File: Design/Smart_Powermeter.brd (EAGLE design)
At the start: 92 x 87 mm, 66 parts, among them IC1 AMS1117-3.3, IC3 ESP32-S2-MINI-1-N4R2, J1 AUDIO_JACK_TRRSSMD_RA, J2 AUDIO_JACK_TRRSSMD_RA, J3 AUDIO_JACK_TRRSSMD_RA, J4 AUDIO_JACK_TRRSSMD_RA, J5 AUDIO_JACK_TRRSSMD_RA, J6 AUDIO_JACK_TRRSSMD_RA, J8 USB-C, Q1 IRLML0100

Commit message: First draft for the Pro version
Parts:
- removed X1: (no value), con-wago-508:W237-132
- added C16, C20, C21: 10u/6V, rcl:C0603
- added D4, D5, D7: ESD5Z3.3T1G, microbuilder:SOD-523
- added F1, F2, F3: 1A x 250V, OpenEnergyMonitor:FUSE
- added JP1, JP2, JP3, JP4, JP5, JP6: JUMPER-SMT_2_NC_TRACE_NO-SILK, SparkFun-Jumpers:SMT-JUMPER_2_NC_TRACE_NO-SILK
- added M1, M2, M3: 275VAC, OpenEnergyMonitor:MOV
- added R21, R22, R23, R24, R26, R27, R28, R32, R33, R34, R35, R38, R39, R40, R48, R49, R50, R51, R52, R53, R54: 10k, rcl:R0603
- added R29, R41, R55: 180k, rcl:R0603
- added R30, R42, R56: 33k, rcl:R0603
- added R31, R43, R57: 1k, rcl:R0603
- added T1, T2, T3: ZMPT101B, OpenEnergyMonitor:ZMPT101B
- added X2: (no value), con-wago-508:W237-5P
- J1, J2, J3, J4, J5, J6: value AUDIO_JACK_TRRSSMD_RA -> AUDIO_JACK_MONO_3.5_3P; device SparkFun-Connectors:AUDIO_JACK_3.5MM_TRRS_SMD_RA -> SpaceDIY_connectors:HC-PJ-320A-3P-D
- R10, R13, R16, R19, R4, R7: device rcl:R1206 -> rcl:R0603
- moved J4 91.5 mm to (51.6, 86.0), turned to 180 degrees
- moved J5 90.5 mm to (62.8, 86.0), turned to 180 degrees
- moved J6 89.7 mm to (74.0, 86.0), turned to 180 degrees
- moved R13 84.0 mm to (46.6, 84.0), flipped to the bottom, turned to 0 degrees
- moved R16 82.9 mm to (57.8, 84.0), flipped to the bottom, turned to 0 degrees
- moved R19 81.9 mm to (69.0, 84.0), flipped to the bottom, turned to 0 degrees
- moved S1 80.3 mm to (76.0, 5.00), turned to 270 degrees
- moved S2 80.3 mm to (58.0, 5.00), turned to 270 degrees
- moved J8 71.0 mm to (67.0, 9.00), turned to 0 degrees
- moved R15 70.7 mm to (57.8, 80.0), flipped to the bottom, turned to 0 degrees
- moved U$2 70.3 mm to (19.0, 44.0), turned to 90 degrees
- moved R18 69.6 mm to (69.0, 80.0), flipped to the bottom, turned to 0 degrees
- moved R12 69.5 mm to (46.6, 80.0), flipped to the bottom, turned to 0 degrees
- moved R11 68.8 mm to (46.6, 78.0), flipped to the bottom, turned to 180 degrees
- moved C4 68.2 mm to (46.6, 76.0), flipped to the bottom, turned to 0 degrees
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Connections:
- removed net VG0: C1.1, J1.EARTH, R2.2, R3.1, R4.1
- new net L1: F1.IN, M1.1, R48.1, U$2.AC1
- new net L2: F2.IN, M2.1, R21.1
- new net L3: F3.IN, M3.1, R32.1
- new net N$10: R23.2, T2.2
- new net N$18: C20.1, R28.1, T2.3
- new net N$19: C20.2, R29.1, R30.2, R31.2
- new net N$20: R32.2, R33.1
- new net N$21: R33.2, R34.1
- new net N$22: R35.1, T3.1
- new net N$23: R35.2, R38.1
- new net N$24: R38.2, R39.1
- new net N$25: R48.2, R49.1
- new net N$26: R34.2, T3.2
- new net N$27: C21.1, R40.1, T3.3
- new net N$28: C21.2, R41.1, R42.2, R43.2
- new net N$29: JP2.2, R7.2
- new net N$3: F2.OUT, X2.2
- new net N$30: JP3.2, R10.2
- new net N$33: JP4.2, R13.2
- new net N$34: JP5.2, R16.2
- new net N$35: JP6.2, R19.2
- new net N$36: R49.2, R50.1
- new net N$37: R51.1, T1.1
- new net N$38: R51.2, R52.1
- new net N$39: R52.2, R53.1
- new net N$4: F3.OUT, X2.3
- new net N$40: R50.2, T1.2
- new net N$41: C16.1, R54.1, T1.3
- new net N$44: C16.2, R55.1, R56.2, R57.2
- new net N$5: R21.2, R22.1
- new net N$6: R22.2, R23.1
- new net N$7: R24.1, T2.1
- new net N$8: R24.2, R26.1
- new net N$9: R26.2, R27.1
- new net NEUTRAL: M1.2, M2.2, M3.2, R27.2, R39.2, R53.2, U$2.AC2, X2.4
- new net V1: D4.K, R57.1
- new net V2: D5.K, R31.1
- new net V3: D7.K, R43.1
- new net VG6: C6.1, J6.1, JP6.1, R17.2, R18.1
- net 3.3V: now also R29.2, R41.2, R55.2
- net GND: now also D4.A, D5.A, D7.A, R28.2, R30.1, R40.2, R42.1, R54.2, R56.1, T1.4, T2.4, T3.4, X2.5
- net M1: now also J1.2, J1.3, R4.1; no longer J1.RING1, J1.RING2, J1.TIP, R4.2
- net M2: now also J2.2, J2.3, R7.1; no longer J2.RING1, J2.RING2, J2.TIP, R7.2
- net M3: now also J3.2, J3.3, R10.1; no longer J3.RING1, J3.RING2, J3.TIP, R10.2
- net M4: now also J4.2, J4.3, R13.1; no longer J4.RING1, J4.RING2, J4.TIP, R13.2
- net M5: now also J5.2, J5.3, R16.1; no longer J5.RING1, J5.RING2, J5.TIP, R16.2
- net M6: now also J6.2, J6.3, R19.1; no longer J6.RING1, J6.RING2, J6.TIP, R19.2
- net N$1: now also JP1.2, R4.2; no longer U$2.AC2, X1.2
- net N$2: now also F1.OUT, X2.1; no longer U$2.AC1, X1.1
- net VG1: now also C1.1, J1.1, JP1.1, R2.2, R3.1; no longer C2.1, J2.EARTH, R5.2, R6.1, R7.1
- net VG2: now also C2.1, J2.1, JP2.1, R5.2, R6.1; no longer C3.1, J3.EARTH, R10.1, R8.2, R9.1
- net VG3: now also C3.1, J3.1, JP3.1, R8.2, R9.1; no longer C4.1, J4.EARTH, R11.2, R12.1, R13.1
- net VG4: now also C4.1, J4.1, JP4.1, R11.2, R12.1; no longer C5.1, J5.EARTH, R14.2, R15.1, R16.1
- net VG5: now also C5.1, J5.1, JP5.1, R14.2, R15.1; no longer C6.1, J6.EARTH, R17.2, R18.1, R19.1
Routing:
- net 3.3V: track 206.4 -> 325.6 mm, vias 5 -> 10
- net NEUTRAL: track 0.00 -> 109.2 mm
- net M4: track 129.1 -> 69.1 mm, vias 4 -> 3
- net L1: track 0.00 -> 57.6 mm
- net M5: track 118.0 -> 60.4 mm, vias 4 -> 3
- net M6: track 104.3 -> 48.4 mm, vias 4 -> 3
- net GND: track 7.30 -> 49.6 mm, vias 6 -> 0
- net RST: track 53.0 -> 80.6 mm, vias 2 -> 1
- net N$4: track 0.00 -> 24.3 mm
- net 5V: track 124.8 -> 148.4 mm, vias 2 -> 4
- net SPI_CS: track 72.0 -> 50.4 mm, vias 4 -> 2
- net SPI_CLK: track 65.4 -> 46.3 mm, vias 4 -> 2
- net SPI_MOSI: track 67.0 -> 49.2 mm, vias 4 -> 2
- net SPI_MISO: track 64.4 -> 46.7 mm
- net N$12: track 31.1 -> 13.7 mm, vias 0 -> 2
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
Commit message: Updated design files
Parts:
- added JP10, JP11, JP12, JP7, JP8, JP9: JUMPER-SMT_2_NO_NO-SILK, SparkFun-Jumpers:SMT-JUMPER_2_NO_NO-SILK
- added JP13: JUMPER-SMT_2_NC_PASTE_NO-SILK, SparkFun-Jumpers:SMT-JUMPER_2_NC_PASTE_NO-SILK
- added LED1: GREEN, SparkFun-LED:LED-0603
- added LED2: BLUE, SparkFun-LED:LED-0603
- added R44: 470, rcl:R0603
- added R45: 330, rcl:R0603
- moved J8 2.00 mm to (67.0, 7.00)
- moved R36 2.00 mm to (70.0, 11.0)
- moved R37 2.00 mm to (64.0, 11.0)
- moved S1 1.58 mm to (76.5, 3.50), turned to 180 degrees
- moved S2 1.58 mm to (57.5, 3.50), turned to 180 degrees
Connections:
- new net LED: IC3.12, R45.2
- new net N$42: LED1.A, R44.1
- new net N$43: JP13.2, R44.2
- new net N$45: LED2.A, R45.1
- new net N$46: J1.2, JP8.2
- new net N$47: J2.2, JP7.2
- new net N$48: J3.2, JP9.2
- new net N$49: J4.2, JP10.2
- new net N$50: J5.2, JP11.2
- new net N$51: J6.2, JP12.2
- net 3.3V: now also JP13.1
- net GND: now also LED1.C, LED2.C
- net M1: now also JP8.1; no longer J1.2
- net M2: now also JP7.1; no longer J2.2
- net M3: now also JP9.1; no longer J3.2
- net M4: now also JP10.1; no longer J4.2
- net M5: now also JP11.1; no longer J5.2
- net M6: now also JP12.1; no longer J6.2
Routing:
- net N$45: track 0.00 -> 35.3 mm, vias 0 -> 1
- net N$42: track 0.00 -> 30.9 mm, vias 0 -> 1
- net LED: track 0.00 -> 17.1 mm, vias 0 -> 2
- net N$17: track 11.0 -> 27.0 mm
- net GND: track 49.6 -> 57.0 mm, vias 0 -> 14
- net N$43: track 0.00 -> 3.04 mm
- net N$49: track 0.00 -> 2.20 mm
- net N$48: track 0.00 -> 2.20 mm
- net N$47: track 0.00 -> 2.20 mm
- net N$46: track 0.00 -> 2.20 mm
- net N$51: track 0.00 -> 2.20 mm
- net N$50: track 0.00 -> 2.20 mm
- net VG6: track 8.96 -> 11.0 mm
- net VG4: track 8.93 -> 10.9 mm
- net VG1: track 8.93 -> 10.9 mm
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
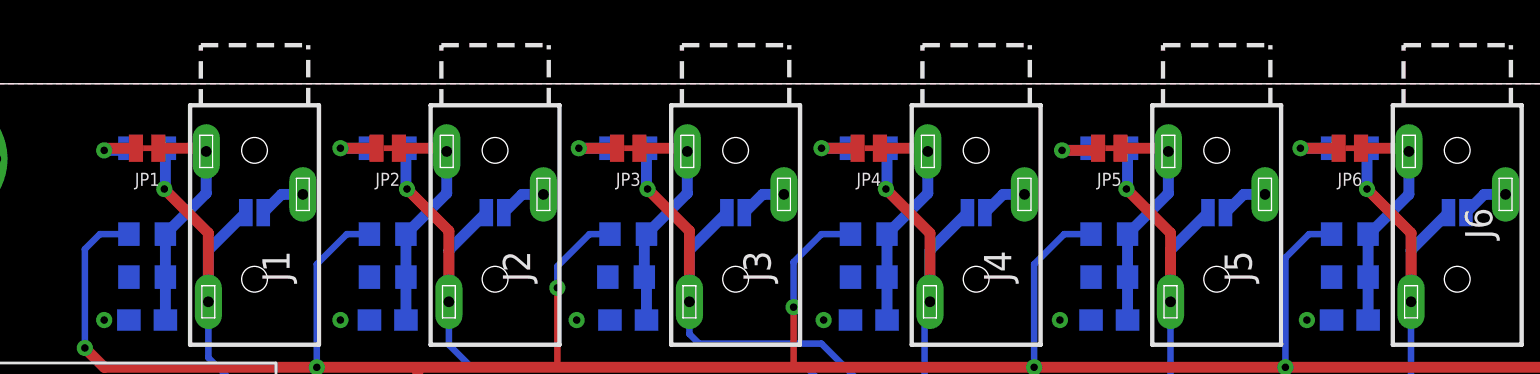
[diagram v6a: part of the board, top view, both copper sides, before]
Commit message: Smart Powermeter Pro with V/I measurements directly on the ESP32-S2
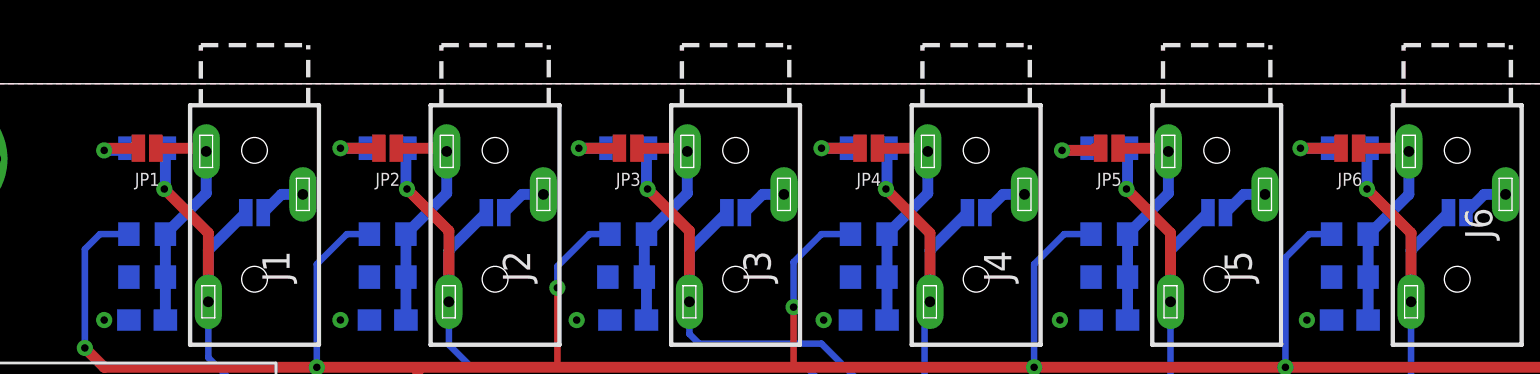
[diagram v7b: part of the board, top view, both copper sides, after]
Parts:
- JP1, JP2, JP3, JP4, JP5, JP6: value JUMPER-SMT_2_NC_TRACE_NO-SILK -> JUMPER-SMT_2_NO_NO-SILK; device SparkFun-Jumpers:SMT-JUMPER_2_NC_TRACE_NO-SILK -> SparkFun-Jumpers:SMT-JUMPER_2_NO_NO-SILK
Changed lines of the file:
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@@
 <attribute name="VALUE" x="48.284" y="39.276" size="0.4064" layer="28" ratio="10" rot="MR0"/>
 </element>
-<element name="JP1" library="SparkFun-Jumpers" package="SMT-JUMPER_2_NC_TRACE_NO-SILK" package3d_urn="urn:adsk.eagle:package:39286/1" value="JUMPER-SMT_2_NC_TRACE_NO-SILK" x="13" y="84" smashed="yes" rot="R180" grouprefs="1">
+<element name="JP1" library="SparkFun-Jumpers" package="SMT-JUMPER_2_NO_NO-SILK" package3d_urn="urn:adsk.eagle:package:39277/1" value="JUMPER-SMT_2_NO_NO-SILK" x="13" y="84" smashed="yes" rot="R180" grouprefs="1">
 <attribute name="NAME" x="13" y="82.857" size="0.6096" layer="25" font="vector" ratio="20" rot="R180" align="bottom-center"/>
 <attribute name="VALUE" x="13" y="85.143" size="0.6096" layer="27" font="vector" ratio="20" rot="R180" align="top-center"/>
@@
 <attribute name="VALUE" x="73" y="80" size="1.27" layer="27" rot="R270" align="center"/>
 </element>
-<element name="JP2" library="SparkFun-Jumpers" package="SMT-JUMPER_2_NC_TRACE_NO-SILK" package3d_urn="urn:adsk.eagle:package:39286/1" value="JUMPER-SMT_2_NC_TRACE_NO-SILK" x="24.2" y="84" smashed="yes" rot="R180" grouprefs="2">
+<element name="JP2" library="SparkFun-Jumpers" package="SMT-JUMPER_2_NO_NO-SILK" package3d_urn="urn:adsk.eagle:package:39277/1" value="JUMPER-SMT_2_NO_NO-SILK" x="24.2" y="84" smashed="yes" rot="R180" grouprefs="2">
 <attribute name="NAME" x="24.2" y="82.857" size="0.6096" layer="25" font="vector" ratio="20" rot="R180" align="bottom-center"/>
 <attribute name="VALUE" x="24.2" y="85.143" size="0.6096" layer="27" font="vector" ratio="20" rot="R180" align="top-center"/>
@@
 <attribute name="VALUE" x="24.835" y="82.095" size="1.27" layer="28" rot="MR0"/>
 </element>
-<element name="JP3" library="SparkFun-Jumpers" package="SMT-JUMPER_2_NC_TRACE_NO-SILK" package3d_urn="urn:adsk.eagle:package:39286/1" value="JUMPER-SMT_2_NC_TRACE_NO-SILK" x="35.4" y="84" smashed="yes" rot="R180" grouprefs="3">
+<element name="JP3" library="SparkFun-Jumpers" package="SMT-JUMPER_2_NO_NO-SILK" package3d_urn="urn:adsk.eagle:package:39277/1" value="JUMPER-SMT_2_NO_NO-SILK" x="35.4" y="84" smashed="yes" rot="R180" grouprefs="3">
 <attribute name="NAME" x="35.4" y="82.857" size="0.6096" layer="25" font="vector" ratio="20" rot="R180" align="bottom-center"/>
 <attribute name="VALUE" x="35.4" y="85.143" size="0.6096" layer="27" font="vector" ratio="20" rot="R180" align="top-center"/>
@@
 <attribute name="VALUE" x="36.035" y="82.095" size="1.27" layer="28" rot="MR0"/>
 </element>
-<element name="JP4" library="SparkFun-Jumpers" package="SMT-JUMPER_2_NC_TRACE_NO-SILK" package3d_urn="urn:adsk.eagle:package:39286/1" value="JUMPER-SMT_2_NC_TRACE_NO-SILK" x="46.6" y="84" smashed="yes" rot="R180" grouprefs="4">
+<element name="JP4" library="SparkFun-Jumpers" package="SMT-JUMPER_2_NO_NO-SILK" package3d_urn="urn:adsk.eagle:package:39277/1" value="JUMPER-SMT_2_NO_NO-SILK" x="46.6" y="84" smashed="yes" rot="R180" grouprefs="4">
 <attribute name="NAME" x="46.6" y="82.857" size="0.6096" layer="25" font="vector" ratio="20" rot="R180" align="bottom-center"/>
 <attribute name="VALUE" x="46.6" y="85.143" size="0.6096" layer="27" font="vector" ratio="20" rot="R180" align="top-center"/>
@@
 <attribute name="VALUE" x="47.235" y="82.095" size="1.27" layer="28" rot="MR0"/>
 </element>
-<element name="JP5" library="SparkFun-Jumpers" package="SMT-JUMPER_2_NC_TRACE_NO-SILK" package3d_urn="urn:adsk.eagle:package:39286/1" value="JUMPER-SMT_2_NC_TRACE_NO-SILK" x="57.8" y="84" smashed="yes" rot="R180" grouprefs="5">
+<element name="JP5" library="SparkFun-Jumpers" package="SMT-JUMPER_2_NO_NO-SILK" package3d_urn="urn:adsk.eagle:package:39277/1" value="JUMPER-SMT_2_NO_NO-SILK" x="57.8" y="84" smashed="yes" rot="R180" grouprefs="5">
 <attribute name="NAME" x="57.8" y="82.857" size="0.6096" layer="25" font="vector" ratio="20" rot="R180" align="bottom-center"/>
 <attribute name="VALUE" x="57.8" y="85.143" size="0.6096" layer="27" font="vector" ratio="20" rot="R180" align="top-center"/>
@@
 <attribute name="VALUE" x="58.435" y="82.095" size="1.27" layer="28" rot="MR0"/>
 </element>
-<element name="JP6" library="SparkFun-Jumpers" package="SMT-JUMPER_2_NC_TRACE_NO-SILK" package3d_urn="urn:adsk.eagle:package:39286/1" value="JUMPER-SMT_2_NC_TRACE_NO-SILK" x="69" y="84" smashed="yes" rot="R180" grouprefs="6">
+<element name="JP6" library="SparkFun-Jumpers" package="SMT-JUMPER_2_NO_NO-SILK" package3d_urn="urn:adsk.eagle:package:39277/1" value="JUMPER-SMT_2_NO_NO-SILK" x="69" y="84" smashed="yes" rot="R180" grouprefs="6">
 <attribute name="NAME" x="69" y="82.857" size="0.6096" layer="25" font="vector" ratio="20" rot="R180" align="bottom-center"/>
 <attribute name="VALUE" x="69" y="85.143" size="0.6096" layer="27" font="vector" ratio="20" rot="R180" align="top-center"/>
@@
 <contactref element="JP1" pad="1"/>
 <contactref element="J1" pad="1"/>
-<wire x1="13.5207" y1="84" x2="15.6" y2="84" width="0.508" layer="1"/>
+<wire x1="13.4064" y1="84" x2="15.6" y2="84" width="0.508" layer="1"/>
 <wire x1="15.6" y1="84" x2="15.75" y2="83.85" width="0.508" layer="1"/>
 <wire x1="15.75" y1="83.85" x2="15.75" y2="81.9" width="0.508" layer="16"/>
@@
 <wire x1="25.05" y1="80" x2="25.05" y2="78" width="0.508" layer="16"/>
 <wire x1="25.05" y1="78" x2="25.05" y2="76" width="0.508" layer="16"/>
-<wire x1="24.7207" y1="84" x2="26.8" y2="84" width="0.508" layer="1"/>
+<wire x1="24.6064" y1="84" x2="26.8" y2="84" width="0.508" layer="1"/>
 <wire x1="26.8" y1="84" x2="26.95" y2="83.85" width="0.508" layer="1"/>
 </signal>
@@
 <contactref element="J3" pad="1"/>
 <contactref element="JP3" pad="1"/>
-<wire x1="35.9207" y1="84" x2="38" y2="84" width="0.508" layer="1"/>
+<wire x1="35.8064" y1="84" x2="38" y2="84" width="0.508" layer="1"/>
 <wire x1="38" y1="84" x2="38.15" y2="83.85" width="0.508" layer="1"/>
 <wire x1="36.25" y1="76" x2="36.25" y2="77.9" width="0.508" layer="16"/>
@@
 <contactref element="J4" pad="1"/>
 <contactref element="JP4" pad="1"/>
-<wire x1="47.1207" y1="84" x2="49.2" y2="84" width="0.508" layer="1"/>
+<wire x1="47.0064" y1="84" x2="49.2" y2="84" width="0.508" layer="1"/>
 <wire x1="49.2" y1="84" x2="49.35" y2="83.85" width="0.508" layer="1"/>
 <wire x1="49.35" y1="83.85" x2="49.35" y2="81.9" width="0.508" layer="16"/>
@@
 <wire x1="60.55" y1="83.85" x2="60.55" y2="81.9" width="0.508" layer="16"/>
 <wire x1="60.55" y1="81.9" x2="58.65" y2="80" width="0.508" layer="16"/>
-<wire x1="58.3207" y1="84" x2="60.4" y2="84" width="0.508" layer="1"/>
+<wire x1="58.2064" y1="84" x2="60.4" y2="84" width="0.508" layer="1"/>
 <wire x1="60.4" y1="84" x2="60.55" y2="83.85" width="0.508" layer="1"/>
 </signal>
@@
 <wire x1="11" y1="83.9" x2="11.1" y2="84" width="0.508" layer="1"/>
 <wire x1="11.1" y1="84" x2="12.3505" y2="84" width="0.508" layer="1"/>
-<wire x1="12.3505" y1="84" x2="12.4793" y2="84" width="0" layer="19" extent="1-1"/>
+<wire x1="12.3505" y1="84" x2="12.5936" y2="84" width="0" layer="19" extent="1-1"/>
 </signal>
 <signal name="VG6">
@@
 <contactref element="J6" pad="1"/>
 <contactref element="JP6" pad="1"/>
-<wire x1="69.5207" y1="84" x2="71.6" y2="84" width="0.508" layer="1"/>
+<wire x1="69.4064" y1="84" x2="71.6" y2="84" width="0.508" layer="1"/>
 <wire x1="71.6" y1="84" x2="71.75" y2="83.85" width="0.508" layer="1"/>
 <wire x1="71.75" y1="83.85" x2="71.75" y2="81.85" width="0.508" layer="16"/>
@@
 <contactref element="R7" pad="2"/>
 <contactref element="JP2" pad="2"/>
-<wire x1="23.6793" y1="84" x2="22" y2="84" width="0.508" layer="1"/>
+<wire x1="23.7936" y1="84" x2="22" y2="84" width="0.508" layer="1"/>
 <via x="22" y="84" extent="1-16" drill="0.35"/>
 <wire x1="22" y1="84" x2="23.35" y2="84" width="0.508" layer="16"/>
@@
 <via x="33.1" y="84" extent="1-16" drill="0.35"/>
 <wire x1="33.1" y1="84" x2="34.7505" y2="84" width="0.508" layer="1"/>
-<wire x1="34.7505" y1="84" x2="34.8793" y2="84" width="0" layer="19" extent="1-1"/>
+<wire x1="34.7505" y1="84" x2="34.9936" y2="84" width="0" layer="19" extent="1-1"/>
 </signal>
 <signal name="N$33">
@@
 <via x="44.4" y="84" extent="1-16" drill="0.35"/>
 <wire x1="44.4" y1="84" x2="45.9505" y2="84" width="0.508" layer="1"/>
-<wire x1="45.9505" y1="84" x2="46.0793" y2="84" width="0" layer="19" extent="1-1"/>
+<wire x1="45.9505" y1="84" x2="46.1936" y2="84" width="0" layer="19" extent="1-1"/>
 </signal>
 <signal name="N$34">
@@
 <wire x1="55.6" y1="83.9" x2="57.0505" y2="83.9" width="0.508" layer="1"/>
 <wire x1="57.0505" y1="83.9" x2="57.1505" y2="84" width="0.508" layer="1"/>
-<wire x1="57.1505" y1="84" x2="57.2793" y2="84" width="0" layer="19" extent="1-1"/>
+<wire x1="57.1505" y1="84" x2="57.3936" y2="84" width="0" layer="19" extent="1-1"/>
 </signal>
 <signal name="N$35">
 <contactref element="R19" pad="2"/>
 <contactref element="JP6" pad="2"/>
-<wire x1="68.4793" y1="84" x2="66.7" y2="84" width="0.508" layer="1"/>
+<wire x1="68.5936" y1="84" x2="66.7" y2="84" width="0.508" layer="1"/>
 <via x="66.7" y="84" extent="1-16" drill="0.35"/>
 <wire x1="66.7" y1="84" x2="68.15" y2="84" width="0.508" layer="16"/>
